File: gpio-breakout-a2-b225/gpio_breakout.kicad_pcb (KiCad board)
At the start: 4 copper layers, 63.5 x 32 mm, 18 parts, among them J1 ZF5S-40-01-T-WT-K-TR, J2 Pi GPIO 2x20, J3 1054500101, U1 LM66100DCKR, U2 TPD2EUSB30DRTR, U3 TPD2EUSB30DRTR

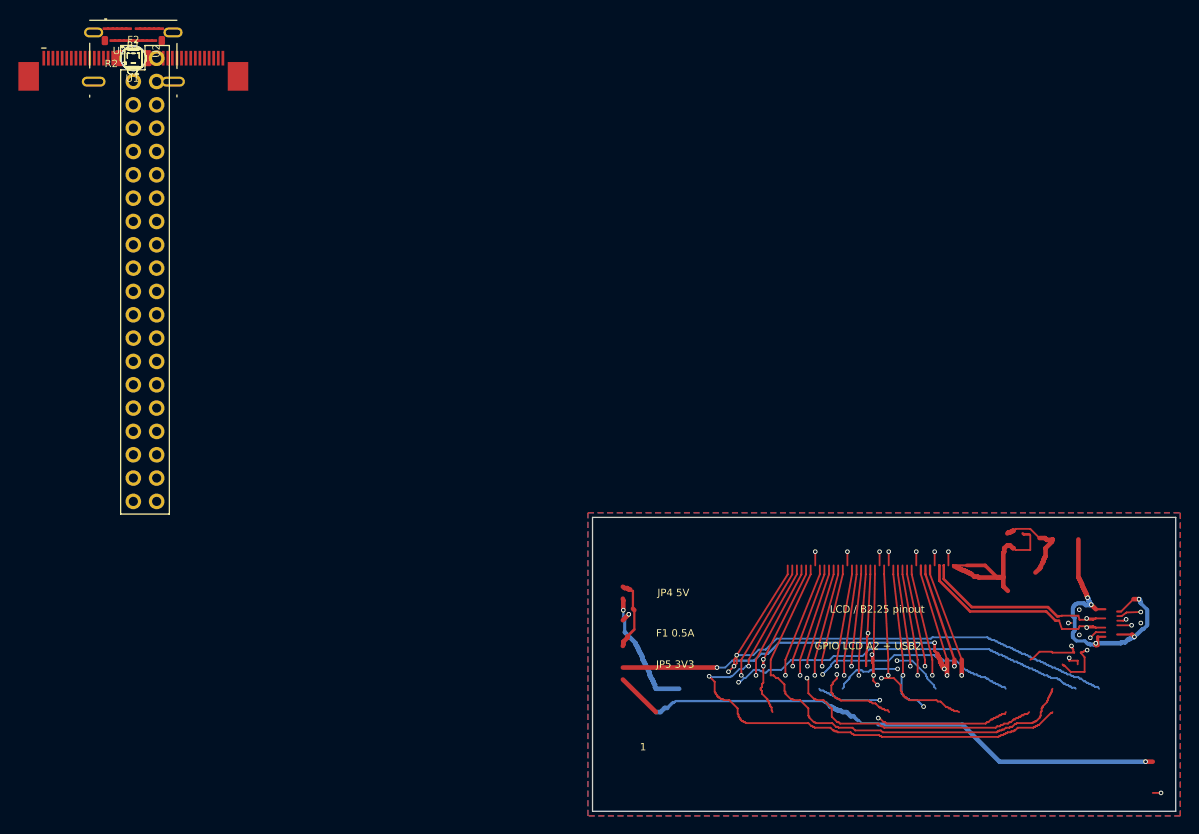
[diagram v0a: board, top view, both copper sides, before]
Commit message: Add GPIO A2 USB soft start and Pi-side display series provisions
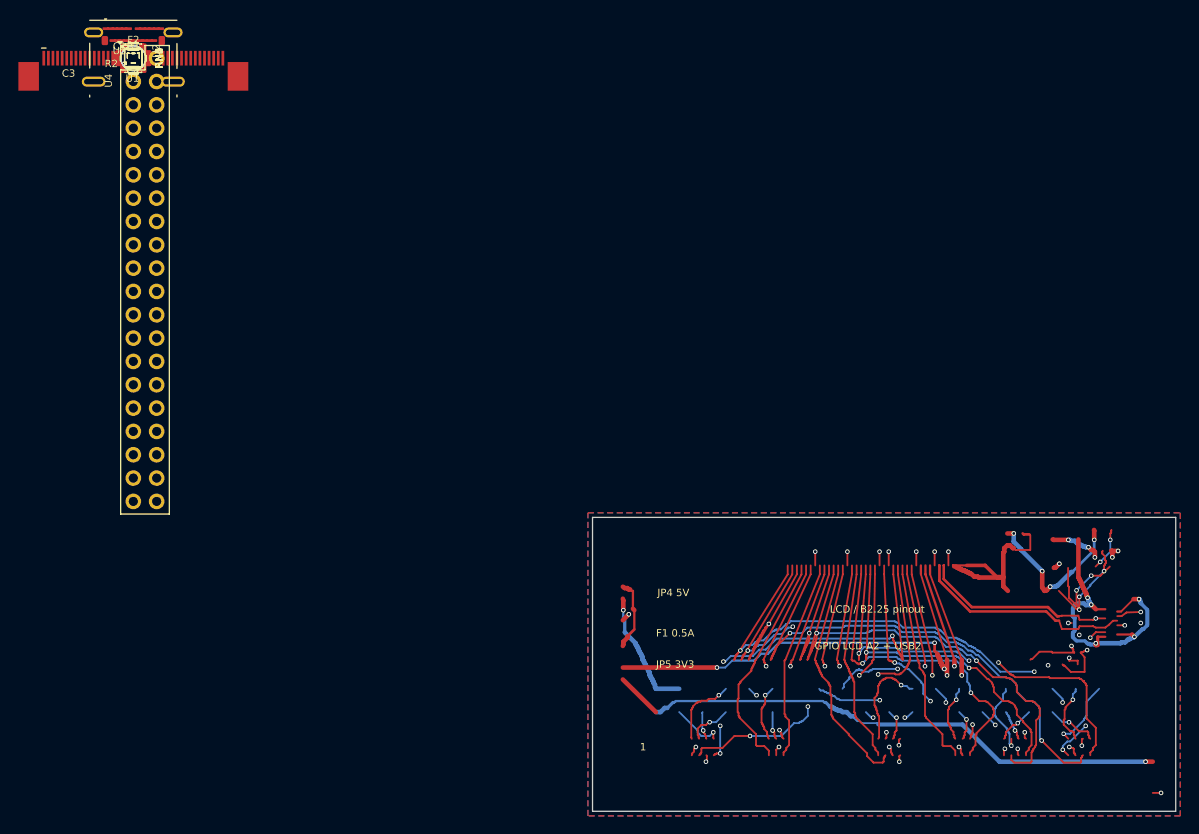
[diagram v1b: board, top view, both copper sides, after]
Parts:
- added C3: 10n 50V C0G 5%, Capacitor_SMD:C_0603_1608Metric, F.Cu at (0.00, 0.00)
- added C4: 1u 16V X7R, Capacitor_SMD:C_0603_1608Metric, F.Cu at (0.00, 0.00)
- added RN1, RN2, RN3, RN4, RN5, RN6: 0R x4 (DPI source option), Resistor_SMD:R_Array_Convex_4x0603, F.Cu at (0.00, 0.00)
- added U4: TPS22918DBVR, Package_TO_SOT_SMD:SOT-23-6, F.Cu at (0.00, 0.00)
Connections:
- J2 pad 10: GPIO15 -> GPIO15_PI
- J2 pad 11: GPIO17 -> GPIO17_PI
- J2 pad 12: GPIO18 -> GPIO18_PI
- J2 pad 19: GPIO10 -> GPIO10_PI
- J2 pad 21: GPIO9 -> GPIO9_PI
- J2 pad 23: GPIO11 -> GPIO11_PI
- J2 pad 24: GPIO8 -> GPIO8_PI
- J2 pad 26: GPIO7 -> GPIO7_PI
- J2 pad 27: ID_SD -> ID_SD_PI
- J2 pad 28: ID_SC -> ID_SC_PI
- J2 pad 29: GPIO5 -> GPIO5_PI
- J2 pad 3: GPIO2 -> GPIO2_PI
- J2 pad 31: GPIO6 -> GPIO6_PI
- J2 pad 32: GPIO12 -> GPIO12_PI
- J2 pad 33: GPIO13 -> GPIO13_PI
- J2 pad 35: GPIO19 -> GPIO19_PI
- J2 pad 36: GPIO16 -> GPIO16_PI
- J2 pad 38: GPIO20 -> GPIO20_PI
- J2 pad 40: GPIO21 -> GPIO21_PI
- J2 pad 5: GPIO3 -> GPIO3_PI
- J2 pad 7: GPIO4 -> GPIO4_PI
- J2 pad 8: GPIO14 -> GPIO14_PI
- J3 pad A10: (no net) -> unconnected-(J3-RX2--PadA10)
- J3 pad A11: (no net) -> unconnected-(J3-RX2+-PadA11)
- J3 pad A2: (no net) -> unconnected-(J3-TX1+-PadA2)
- J3 pad A3: (no net) -> unconnected-(J3-TX1--PadA3)
- J3 pad A8: (no net) -> unconnected-(J3-SBU1-PadA8)
- J3 pad B10: (no net) -> unconnected-(J3-RX1--PadB10)
- J3 pad B11: (no net) -> unconnected-(J3-RX1+-PadB11)
- J3 pad B2: (no net) -> unconnected-(J3-TX2+-PadB2)
- J3 pad B3: (no net) -> unconnected-(J3-TX2--PadB3)
- J3 pad B8: (no net) -> unconnected-(J3-SBU2-PadB8)
- U1 pad 1: USB_VBUS_IN -> USB_VBUS_SOFT
- U1 pad 4: (no net) -> unconnected-(U1-NC-Pad4)
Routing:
- net GND: track 13.4 -> 36.3 mm, vias 13 -> 18
- net USB_VBUS_SOFT: track 0.00 -> 17.8 mm, vias 0 -> 4
- net GPIO12: track 35.9 -> 51.5 mm
- net GPIO7: track 22.0 -> 36.0 mm
- net GPIO8_PI: track 0.00 -> 10.9 mm, vias 0 -> 1
- net GPIO18: track 15.6 -> 24.6 mm, vias 1 -> 0
- net GPIO13: track 41.9 -> 50.8 mm
- net GPIO16_PI: track 0.00 -> 8.36 mm, vias 0 -> 2
- net GPIO7_PI: track 0.00 -> 8.26 mm, vias 0 -> 2
- net GPIO12_PI: track 0.00 -> 8.20 mm, vias 0 -> 1
- net GPIO10: track 19.2 -> 27.3 mm, vias 1 -> 2
- net GPIO14_PI: track 0.00 -> 8.00 mm, vias 0 -> 1
- net GPIO14: track 21.5 -> 29.2 mm, vias 1 -> 2
- net GPIO21_PI: track 0.00 -> 7.63 mm, vias 0 -> 1
- net GPIO15_PI: track 0.00 -> 7.34 mm, vias 0 -> 2
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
